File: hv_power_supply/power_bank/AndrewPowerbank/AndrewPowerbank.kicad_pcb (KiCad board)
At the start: 2 copper layers, 48.3 x 30.5 mm, 43 parts, among them J1 CONN_01x02, J2 CONN_01x02, J3 USB-A-S-X-X-SM2, J4 USB-Micro-1981568-1, Q1 SSM3K333R, U2 MCP73871T-2CCI_ML, U3 TPS61090RSAR

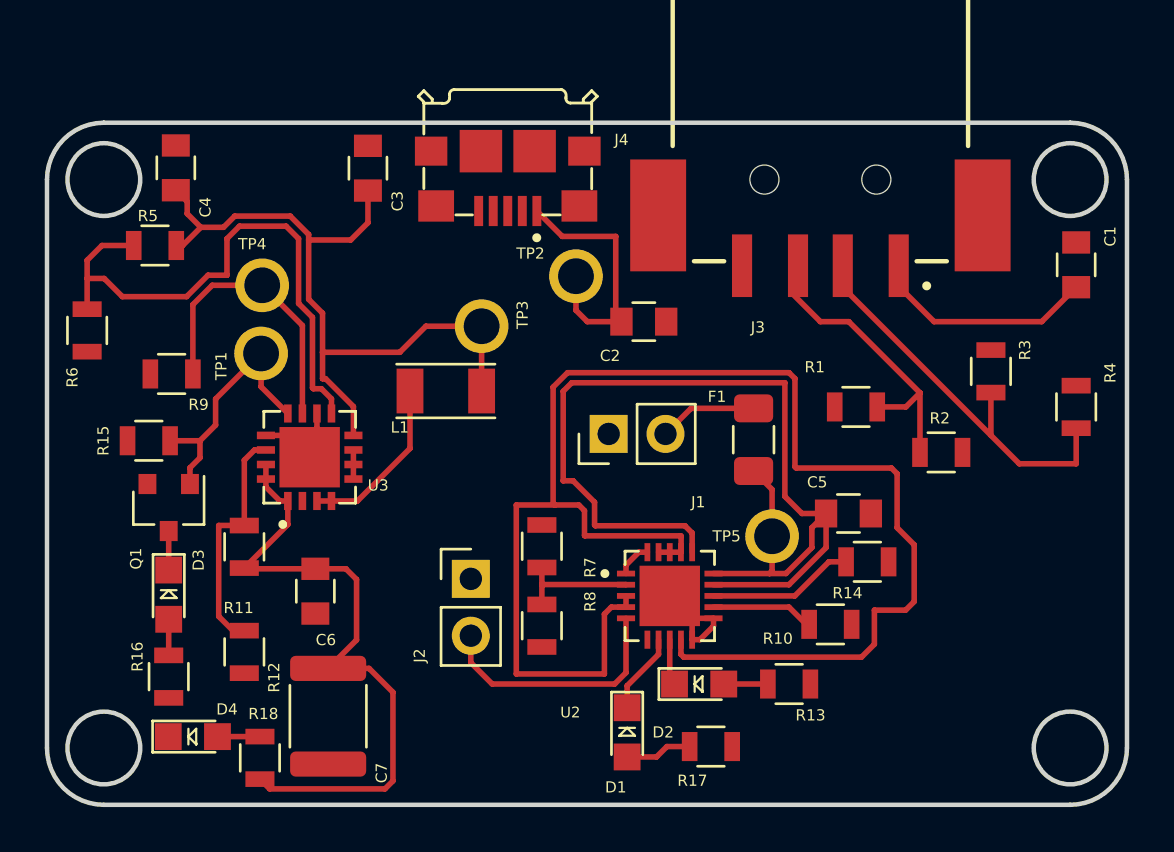
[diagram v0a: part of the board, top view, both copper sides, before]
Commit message: Fixed issues regarding R15, R16 connections, acute trace connections. Added via pathways. \ R15 is now a 1M pull-up resistor connected to VOUT lines on U3 component after C6, C7 components, before R18. Former +BATT connection to R16 is now +5V. Added vias & pathways connecting +5V, VBUS, BATT+, GND nets.
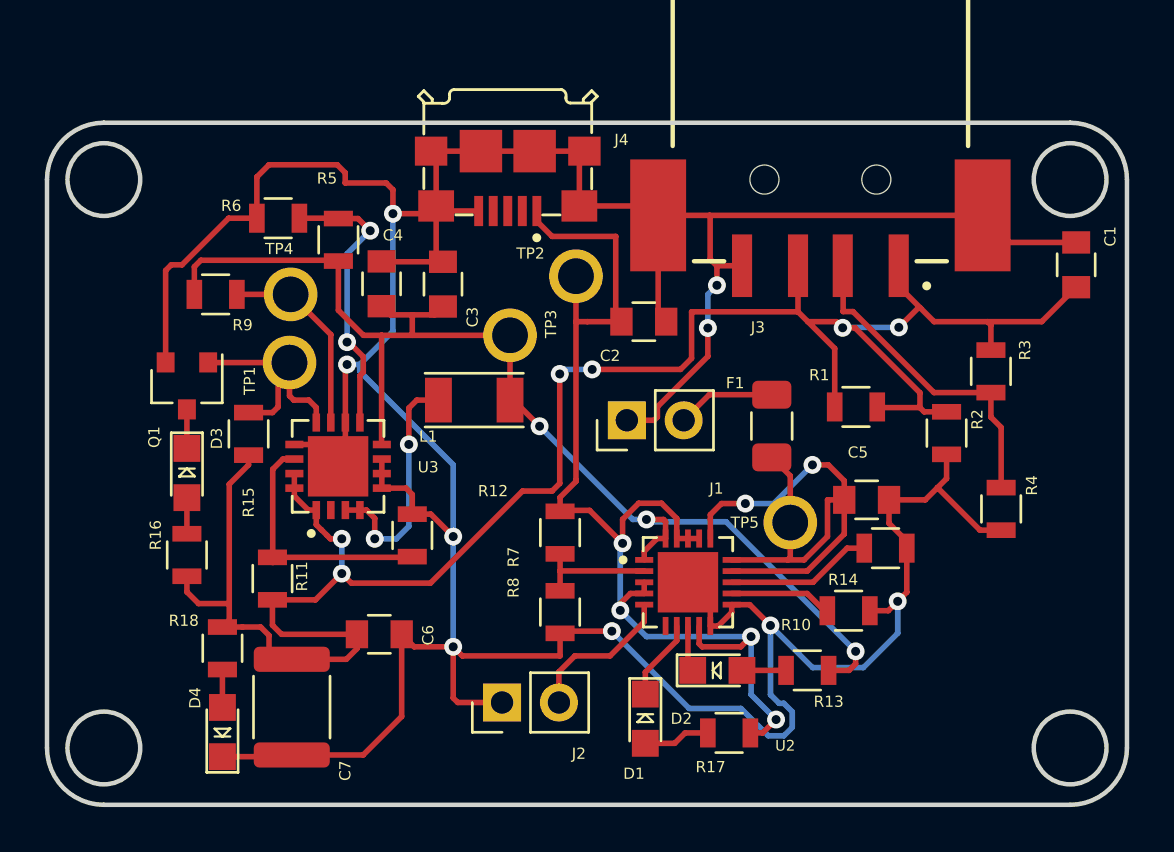
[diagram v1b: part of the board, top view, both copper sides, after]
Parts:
- R15: value R_10K -> R_1M
- moved C4 10.6 mm to (83.3, 66.9)
- moved R6 9.90 mm to (78.6, 64.0), turned to 180 degrees
- moved R12 9.14 mm to (84.6, 78.1), turned to 270 degrees
- moved R5 8.20 mm to (81.3, 64.9), turned to 270 degrees
- moved C3 6.17 mm to (86.0, 66.9)
- moved J2 5.70 mm to (88.6, 85.6), turned to 90 degrees
- moved R4 5.66 mm to (110.9, 76.9), turned to 90 degrees
- moved Q1 5.50 mm to (74.6, 71.5)
- moved R16 5.50 mm to (74.6, 79.0)
- moved D3 5.50 mm to (74.6, 75.3)
- moved R18 5.18 mm to (76.1, 83.2), turned to 270 degrees
- moved R15 4.47 mm to (77.3, 73.6), turned to 90 degrees
- moved R9 4.06 mm to (75.8, 67.4)
- moved C6 3.45 mm to (83.2, 82.5), turned to 0 degrees
- moved R11 1.90 mm to (78.4, 80.1)
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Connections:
- R15 pad 1: Net-(Q1-Pad1) -> +5V
- R15 pad 2: GND -> Net-(Q1-Pad1)
- R16 pad 1: +BATT -> +5V
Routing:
- net GND: track 9.25 -> 187.4 mm, vias 0 -> 9
- net +5V: track 53.4 -> 96.5 mm, vias 0 -> 6
- net VBUS: track 81.8 -> 50.8 mm, vias 0 -> 4
- net /Battery+: track 48.4 -> 28.4 mm, vias 0 -> 2
- net +BATT: track 35.3 -> 55.1 mm, vias 0 -> 3
- net Net-(R5-Pad1): track 25.4 -> 12.8 mm, vias 0 -> 2
- net /16KThermistor: track 11.2 -> 6.87 mm
- net Net-(R9-Pad1): track 13.0 -> 8.88 mm
- net Net-(L1-Pad2): track 7.70 -> 11.3 mm, vias 0 -> 2
- net Net-(J3-Pad02): track 16.5 -> 14.6 mm
- net Net-(Q1-Pad1): track 11.7 -> 10.8 mm

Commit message: 1st Rev of Andrew's Personal Onboarding Project
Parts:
- added C3: C_4.7uF, footprints:C_0603_1608Metric, F.Cu at (111.5, 83.3)
- added C5: C_4.7uF, footprints:C_0603_1608Metric, F.Cu at (96.1, 76.4)
- added C7: C_4.7uF, footprints:C_0603_1608Metric, F.Cu at (92.2, 75.5)
- added C8: C_10pF, footprints:C_0603_1608Metric, F.Cu at (87.5, 81.1)
- renumbered C7 to C10, C3 to C6, C6 to C9, D2 to D1, D1 to D2, J2 to J1, J1 to J2, R13 to R11, R17 to R12, R14 to R13, R11 to R14, R12 to R15, R15 to R17, R7 to R5, R8 to R6, R5 to R7, R6 to R8, TP2 to TP1, TP5 to TP2, TP1 to TP5, U2 to U1, U3 to U2
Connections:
- R11 pad 1: +BATT -> VBUS
- U1 pad 1: +BATT -> Net-(C7-Pad1)
- U1 pad 10: GND -> Net-(U1-Pad10)
- U1 pad 18: VBUS -> Net-(C5-Pad2)
- U1 pad 19: VBUS -> Net-(C5-Pad2)
- U1 pad 20: +BATT -> Net-(U1-Pad20)
- U1 pad 21: GND -> Net-(U1-Pad10)
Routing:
- net GND: track 187.4 -> 133.4 mm
- net +BATT: track 55.1 -> 41.6 mm, vias 3 -> 2
- net VBUS: track 50.8 -> 55.0 mm
- added copper zone on B.Cu, net GND

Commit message: Revamp first-year onboarding project board after feedback.
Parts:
- removed the C5 at (96.1, 76.4)
- removed the C5 at (104.9, 76.5)
- added C5: C_4.7uF, footprints:C_0603_1608Metric, F.Cu at (54.6, 93.1)
- added J5: NanoFit_RA_TH_02, footprints:NanoFit_Molex_1x02x2.50mm_Angled_OEM, F.Cu at (57.4, 100.1)
- J1, J2: value CONN_01x02 -> NanoFit_RA_TH_02; footprint Connector_PinHeader_2.54mm:PinHeader_1x02_P2.54mm_Vertical -> footprints:NanoFit_Molex_1x02x2.50mm_Angled_OEM
- moved C3 55.7 mm to (56.0, 88.6), turned to 90 degrees
- moved C2 55.3 mm to (41.0, 81.0), turned to 0 degrees
- moved TP4 53.8 mm to (33.3, 95.4), turned to 0 degrees
- moved R7 51.4 mm to (35.3, 87.8), turned to 90 degrees
- moved R8 51.4 mm to (35.3, 91.5), turned to 270 degrees
- moved C4 50.2 mm to (35.3, 81.8)
- moved C6 50.2 mm to (38.0, 81.8)
- moved TP5 49.9 mm to (37.7, 98.1), turned to 180 degrees
- moved TP1 49.5 mm to (43.9, 78.5)
- moved J4 49.5 mm to (40.9, 73.3)
- moved TP2 49.3 mm to (53.5, 89.1), turned to 180 degrees
- moved R9 49.3 mm to (33.3, 92.3), turned to 90 degrees
- moved C8 48.1 mm to (41.2, 94.3), turned to 270 degrees
- moved R13 48.0 mm to (58.8, 88.3), turned to 90 degrees
- moved R2 47.8 mm to (61.5, 81.9), turned to 180 degrees
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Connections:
- U1 pad 20: Net-(U1-Pad20) -> Net-(C7-Pad1)
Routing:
- net GND: track 133.4 -> 117.5 mm, vias 9 -> 21
- net Net-(Q1-Pad1): track 10.8 -> 22.1 mm, vias 0 -> 1
- net /Battery+: track 28.4 -> 18.2 mm, vias 2 -> 1
- net +5V: track 96.5 -> 86.6 mm, vias 6 -> 4
- net Net-(J3-Pad02): track 14.6 -> 5.98 mm
- net Net-(R7-Pad1): track 12.8 -> 4.34 mm, vias 2 -> 0
- net Net-(F1-Pad1): track 4.41 -> 12.2 mm, vias 0 -> 1
- net Net-(L1-Pad2): track 11.3 -> 3.59 mm, vias 2 -> 0
- net VBUS: track 55.0 -> 60.2 mm, vias 4 -> 3
- net Net-(R13-Pad1): track 6.56 -> 1.62 mm
- net +BATT: track 41.6 -> 45.8 mm, vias 2 -> 1
- net Net-(C5-Pad2): track 0.00 -> 3.65 mm
- net Net-(C7-Pad1): track 0.00 -> 3.53 mm
- net Net-(U1-Pad10): track 0.00 -> 2.37 mm
- net Net-(R9-Pad1): track 8.88 -> 11.1 mm, vias 0 -> 1
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- added copper zone on F.Cu, net +5V
- added copper zone on F.Cu, net +BATT
- added copper zone on F.Cu, net GND
- added copper zone on F.Cu, net Net-(C8-Pad2)
- added copper zone on F.Cu, net Net-(L1-Pad2)
- added copper zone on F.Cu, net Net-(R7-Pad1)

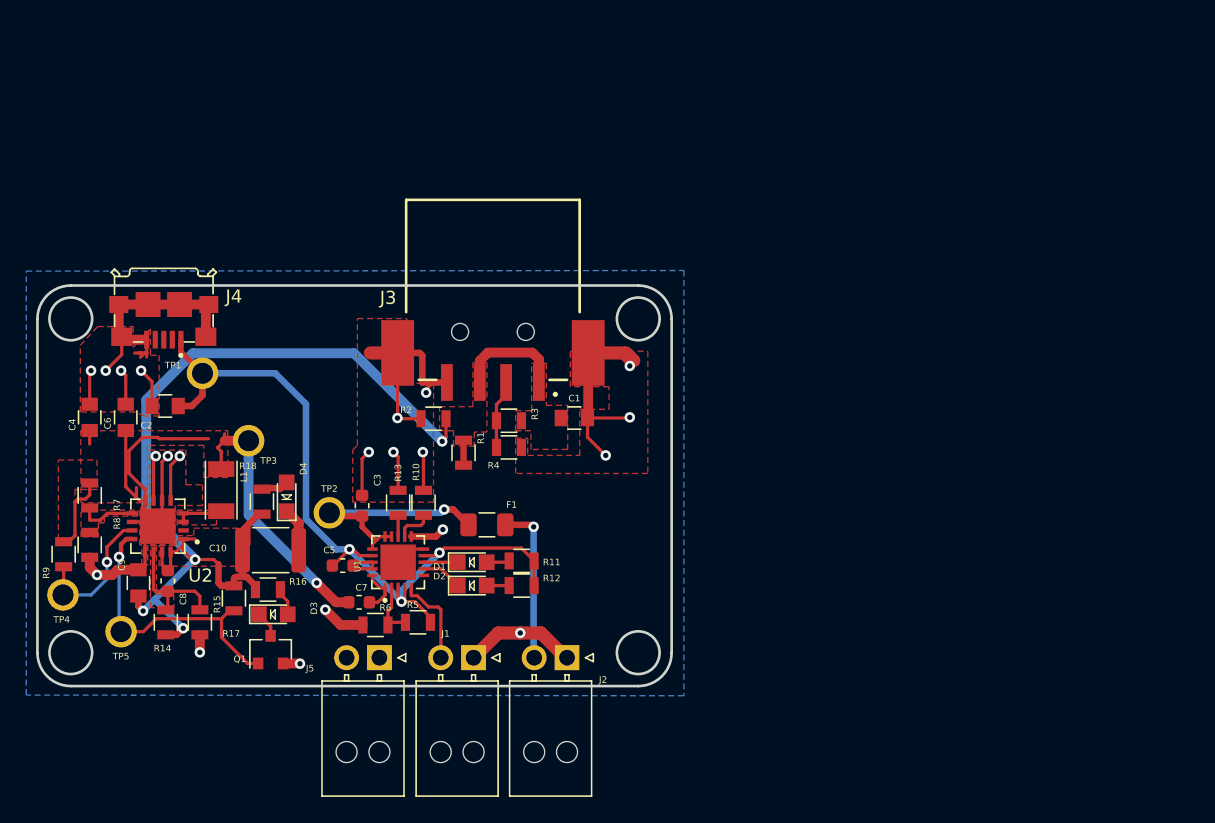
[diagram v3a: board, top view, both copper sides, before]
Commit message: Add switch connections, labels to LEDs, name / date.
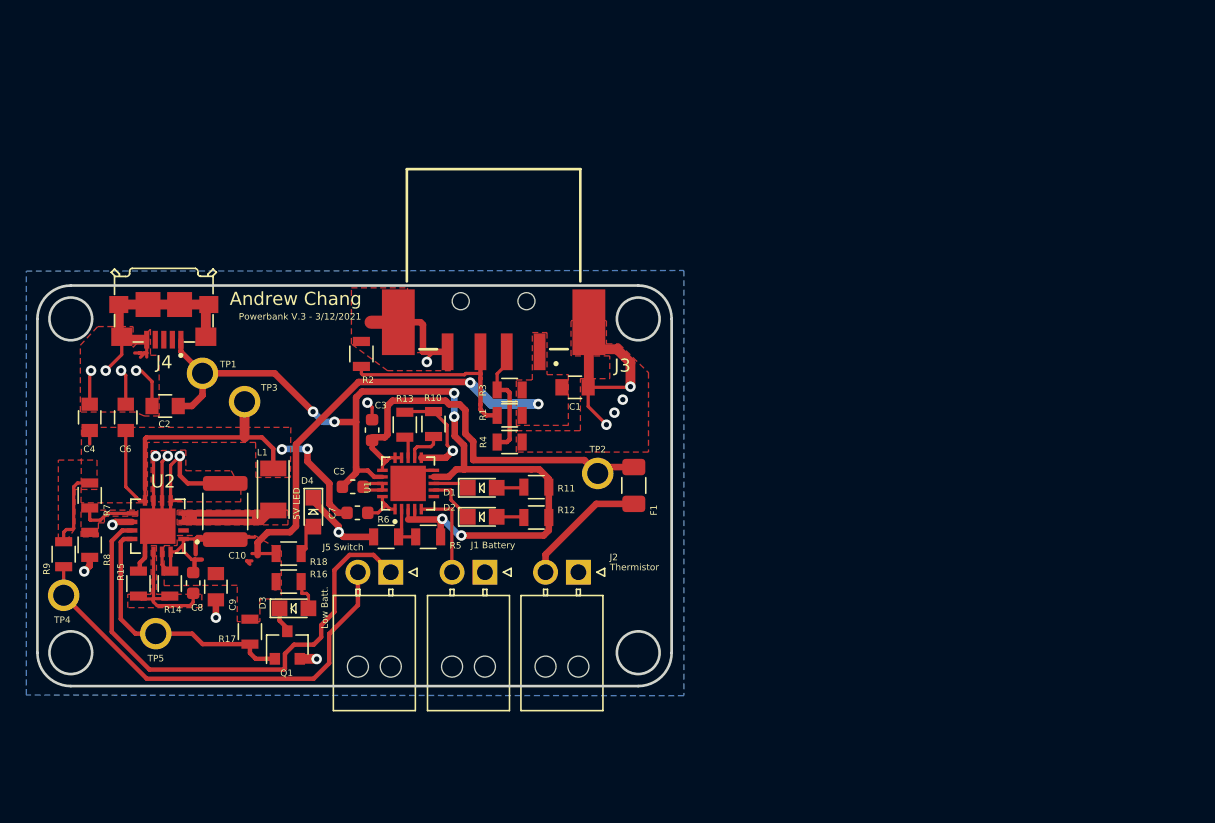
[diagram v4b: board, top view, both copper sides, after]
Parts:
- moved TP2 20.6 mm to (74.0, 86.1)
- moved F1 11.6 mm to (76.7, 87.0), turned to 90 degrees
- moved R2 7.37 mm to (56.0, 77.0), turned to 90 degrees
- moved C7 6.81 mm to (55.7, 89.1)
- moved R6 6.75 mm to (57.9, 90.9)
- moved J2 6.56 mm to (72.5, 93.6)
- moved J1 6.56 mm to (65.4, 93.6)
- moved J5 6.56 mm to (58.2, 93.6)
- moved R5 6.55 mm to (61.1, 90.9)
- moved C5 6.04 mm to (55.3, 87.1)
- moved R10 6.04 mm to (61.5, 82.3)
- moved U1 6.04 mm to (59.5, 86.9)
- moved R13 5.97 mm to (59.3, 82.4)
- moved C9 5.90 mm to (44.9, 94.7), turned to 270 degrees
- moved C3 5.81 mm to (56.8, 82.8)
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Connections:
- J3 pad 03: +5V -> Net-(J3-Pad03)
- R1 pad 2: +5V -> Net-(J3-Pad03)
- R2 pad 1: +5V -> Net-(J3-Pad03)
- R9 pad 1: Net-(R9-Pad1) -> Net-(J5-Pad2)
- TP4 pad 1: Net-(R9-Pad1) -> Net-(J5-Pad2)
- U2 pad 11: Net-(R9-Pad1) -> Net-(J5-Pad1)
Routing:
- net Net-(J5-Pad1): track 0.00 -> 38.4 mm
- net +5V: track 86.6 -> 51.9 mm, vias 4 -> 2
- net Net-(J5-Pad2): track 0.00 -> 33.4 mm
- net Net-(L1-Pad2): track 3.59 -> 19.7 mm
- net Net-(J3-Pad03): track 0.00 -> 15.5 mm
- net /Battery+: track 18.2 -> 31.1 mm, vias 1 -> 0
- net VBUS: track 60.2 -> 72.3 mm, vias 3 -> 6
- net Net-(R9-Pad1): track 11.1 -> 0.00 mm, vias 1 -> 0
- net GND: track 117.5 -> 106.9 mm, vias 21 -> 19
- net +BATT: track 45.8 -> 40.8 mm, vias 1 -> 2
- net Net-(J3-Pad02): track 5.98 -> 9.57 mm
- net Net-(F1-Pad1): track 12.2 -> 9.66 mm, vias 1 -> 0
- net Net-(C8-Pad2): track 9.17 -> 10.3 mm
- net Net-(R5-Pad1): track 4.83 -> 3.81 mm
- net Net-(Q1-Pad1): track 22.1 -> 21.1 mm, vias 1 -> 0
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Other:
- board text added: "5V LED"
- board text added: "Andrew Chang"
- board text added: "Battery"
- board text added: "Low Batt."
- board text added: "Powerbank V.3 - 3/12/2021"
- board text added: "Switch"
- board text added: "Thermistor"

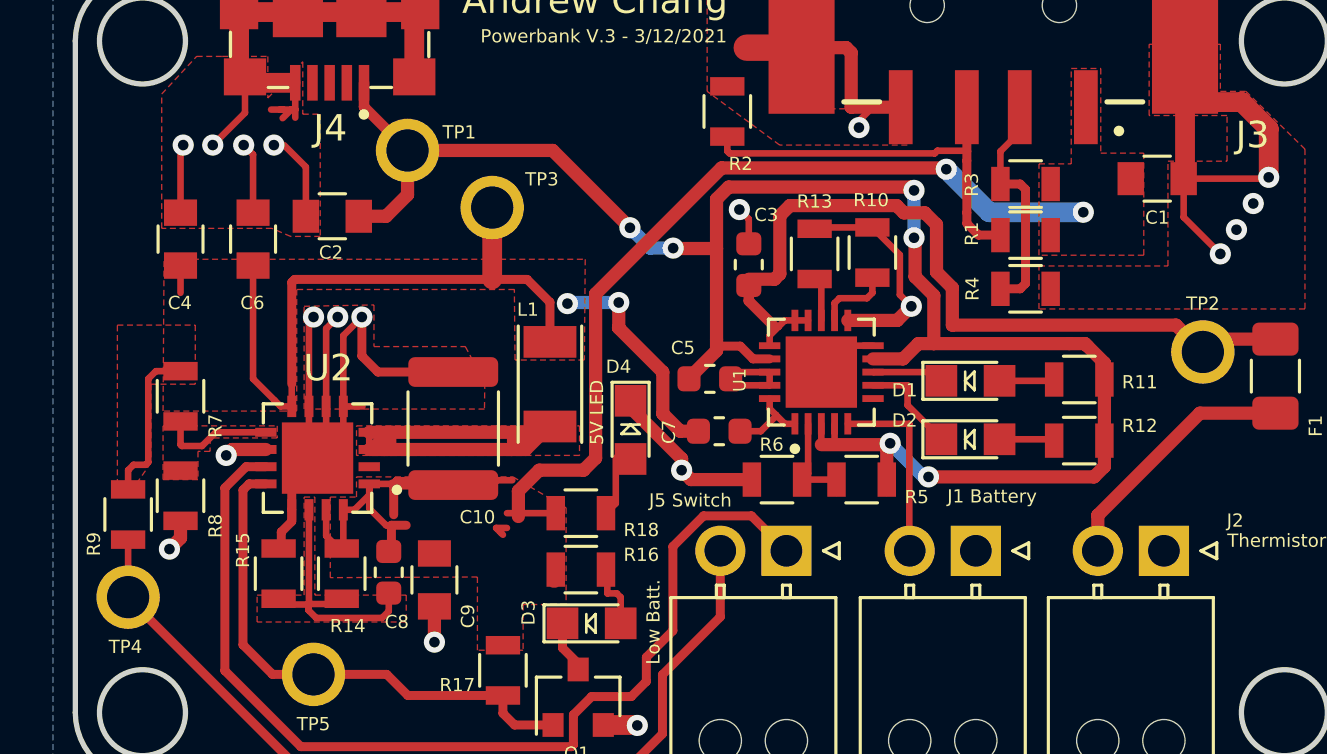
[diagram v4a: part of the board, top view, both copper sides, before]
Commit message: Address DRC pad connection issues.
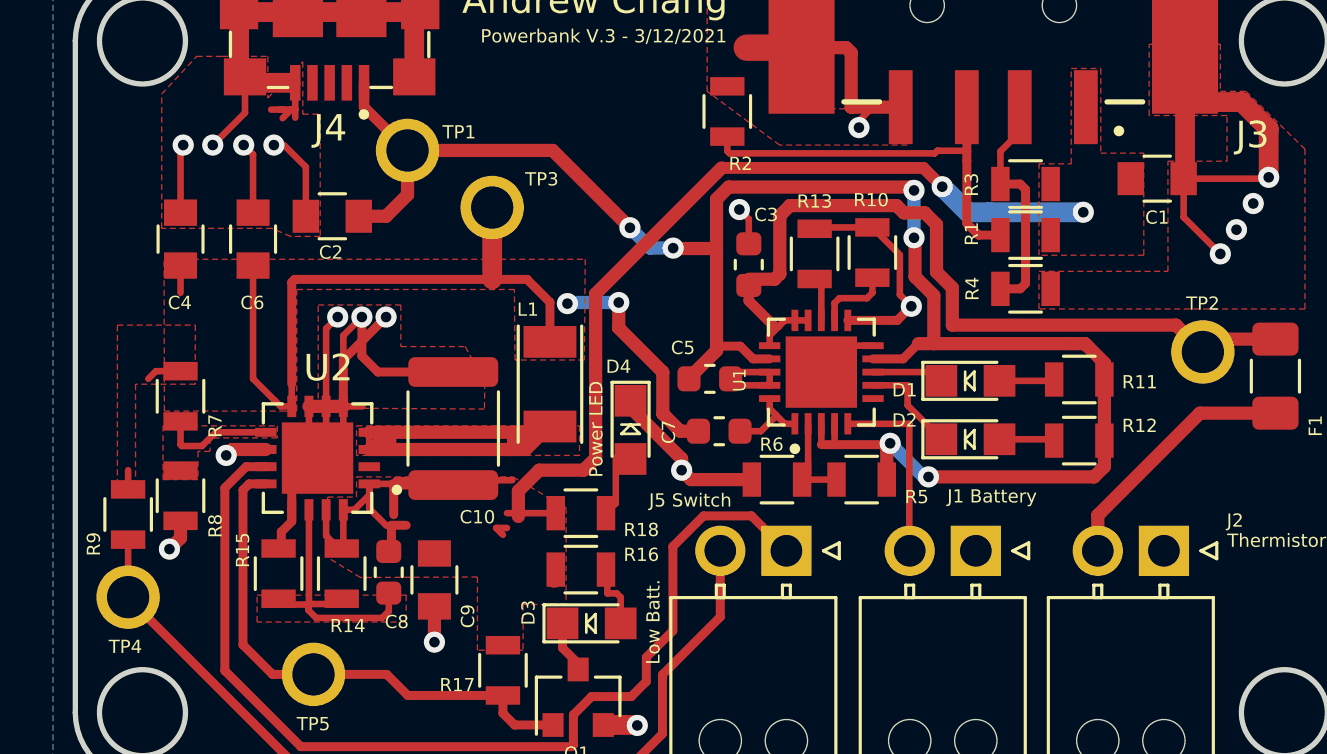
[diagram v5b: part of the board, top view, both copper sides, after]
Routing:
- net +BATT: track 40.8 -> 36.8 mm
- net GND: track 106.9 -> 108.8 mm
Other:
- board text added: "Power LED"
- board text removed: "5V LED"
